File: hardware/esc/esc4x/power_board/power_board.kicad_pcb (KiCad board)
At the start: 4 copper layers, 44 x 46.5 mm, 107 parts, among them J1 Conn_01x06_MountingPin, J10 Conn_01x03_Pin, J2 Conn_01x01, J3 Conn_01x01, J4 Conn_01x03_Pin, J5 Conn_01x03_Pin, J6 Conn_01x03_Pin, Q1 BSC010N04LS6, Q10 BSC010N04LS6, Q11 BSC010N04LS6, Q12 BSC010N04LS6, Q13 BSC010N04LS6, Q14 BSC010N04LS6, Q15 BSC010N04LS6, Q16 BSC010N04LS6, Q17 BSC010N04LS6, Q18 BSC010N04LS6, Q19 BSC010N04LS6, Q2 BSC010N04LS6, Q20 BSC010N04LS6, Q21 BSC010N04LS6, Q22 BSC010N04LS6, Q23 BSC010N04LS6, Q24 BSC010N04LS6, Q3 BSC010N04LS6, Q4 BSC010N04LS6, Q5 BSC010N04LS6, Q6 BSC010N04LS6, Q7 BSC010N04LS6, Q8 BSC010N04LS6, Q9 BSC010N04LS6, U2 AP7381-50Y-13, U3 AP7381-33SA-7, U4 AP7381-50Y-13, U5 AP7381-50Y-13, U7 AP7381-33SA-7, U8 AP7381-50Y-13

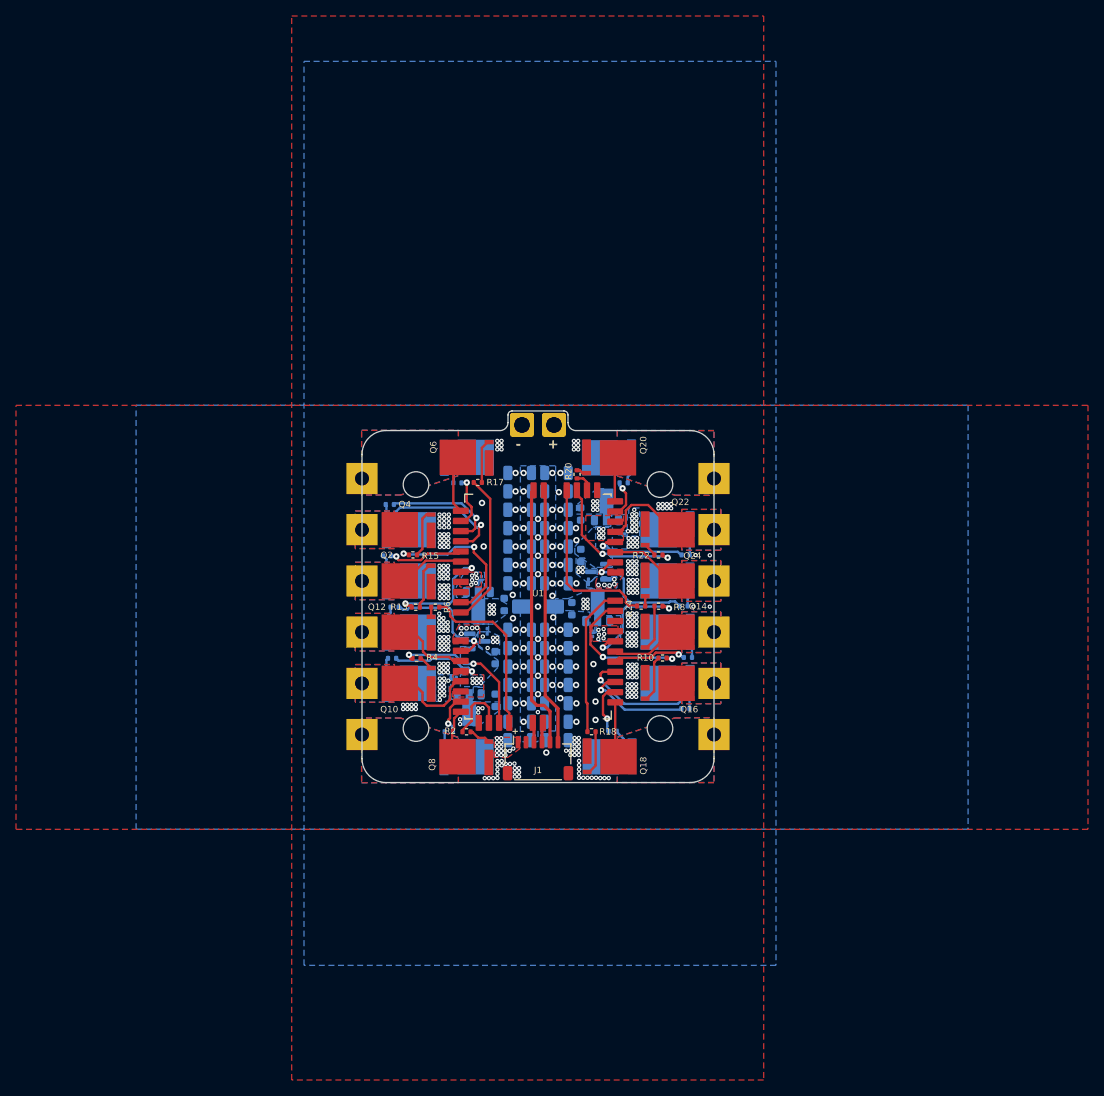
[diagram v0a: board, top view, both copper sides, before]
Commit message: Wider ESC battery holes
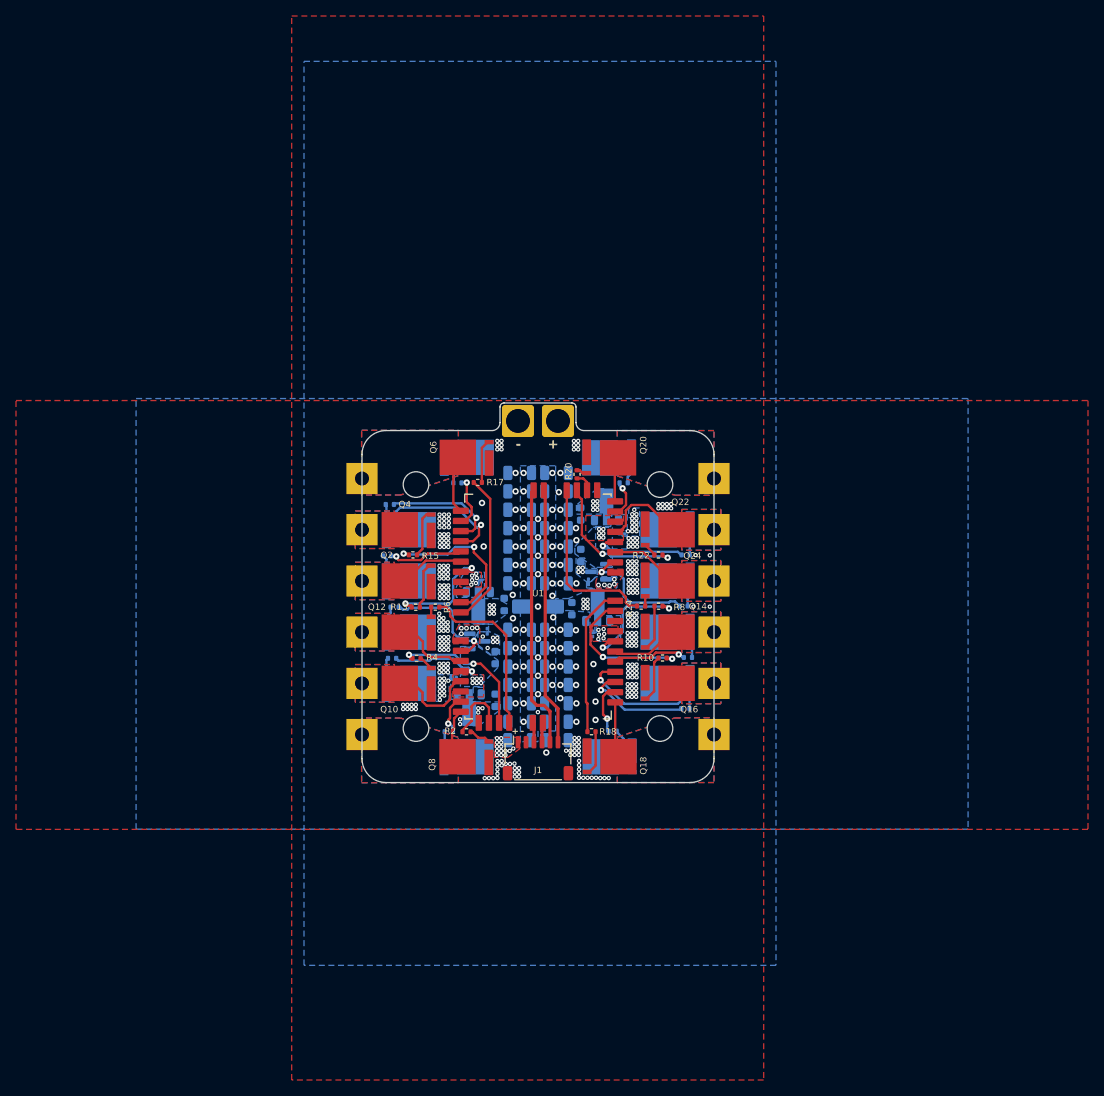
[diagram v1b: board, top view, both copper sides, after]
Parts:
- moved J2 0.71 mm to (152.5, 76.8)
- moved J3 0.71 mm to (147.5, 76.8)
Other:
- board size 44 x 46.5 mm -> 44 x 47.5 mm
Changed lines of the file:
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@@
 	(footprint "Custom:EscBatteryConnector"
 		(layer "F.Cu")
-		(at 152 77.3 90)
+		(at 152.5 76.8 90)
 		(descr "Soldered wire connection, for a single 1 mm² wire, basic insulation, conductor diameter 1.4mm, outer diameter 2.7mm, size source Multi-Contact FLEXI-E 1.0 (https://www.staubli.com/content/dam/ecs/catalogs-brochures/TM/CAB-Main-11014119-en.pdf#page=9), bend radius 3 times outer diameter, generated with kicad-footprint-generator")
 		(tags "connector wire 1sqmm")
@@
 		(sheetname "/")
 		(sheetfile "power_board.kicad_sch")
-		(units
-			(unit
-				(name "A")
-				(pins "1")
-			)
-		)
 		(attr exclude_from_bom)
 		(duplicate_pad_numbers_are_jumpers no)
@@
 		(pad "1" thru_hole roundrect
 			(at 0 0 90)
-			(size 3 3)
-			(drill 2)
+			(size 4 4)
+			(drill 3)
 			(layers "*.Cu" "*.Mask")
 			(remove_unused_layers no)
@@
 	(footprint "Custom:EscBatteryConnector"
 		(layer "F.Cu")
-		(at 148 77.3 90)
+		(at 147.5 76.8 90)
 		(descr "Soldered wire connection, for a single 1 mm² wire, basic insulation, conductor diameter 1.4mm, outer diameter 2.7mm, size source Multi-Contact FLEXI-E 1.0 (https://www.staubli.com/content/dam/ecs/catalogs-brochures/TM/CAB-Main-11014119-en.pdf#page=9), bend radius 3 times outer diameter, generated with kicad-footprint-generator")
 		(tags "connector wire 1sqmm")
@@
 		(sheetname "/")
 		(sheetfile "power_board.kicad_sch")
-		(units
-			(unit
-				(name "A")
-				(pins "1")
-			)
-		)
 		(attr exclude_from_bom)
 		(duplicate_pad_numbers_are_jumpers no)
@@
 		(pad "1" thru_hole roundrect
 			(at 0 0 90)
-			(size 3 3)
-			(drill 2)
+			(size 4 4)
+			(drill 3)
 			(layers "*.Cu" "*.Mask")
 			(remove_unused_layers no)
@@
 	(gr_line
 		(start 131 78)
-		(end 145.25 78)
+		(end 144.25 78)
 		(stroke
 			(width 0.05)
@@
 		(layer "Edge.Cuts")
 	)
-	(gr_line
-		(start 146 122)
-		(end 131 122)
+	(gr_arc
+		(start 145.25 75.05)
+		(mid 145.396447 74.696447)
+		(end 145.75 74.55)
 		(stroke
 			(width 0.05)
@@
 	)
 	(gr_arc
-		(start 146.25 76.05)
-		(mid 146.396447 75.696447)
-		(end 146.75 75.55)
+		(start 145.25 77)
+		(mid 144.957107 77.707107)
+		(end 144.25 78)
 		(stroke
 			(width 0.05)
@@
 		(layer "Edge.Cuts")
 	)
-	(gr_arc
-		(start 146.25 77)
-		(mid 145.957107 77.707107)
-		(end 145.25 78)
+	(gr_line
+		(start 145.25 77)
+		(end 145.25 75.05)
 		(stroke
 			(width 0.05)
@@
 	)
 	(gr_line
-		(start 146.25 77)
-		(end 146.25 76.05)
+		(start 145.75 74.55)
+		(end 154.25 74.55)
 		(stroke
 			(width 0.05)
@@
 	)
 	(gr_line
-		(start 146.75 75.55)
-		(end 153.25 75.55)
+		(start 146 122)
+		(end 131 122)
 		(stroke
 			(width 0.05)
@@
 	)
 	(gr_arc
-		(start 153.25 75.55)
-		(mid 153.603553 75.696447)
-		(end 153.75 76.05)
+		(start 154.25 74.55)
+		(mid 154.603553 74.696447)
+		(end 154.75 75.05)
 		(stroke
 			(width 0.05)
@@
 	)
 	(gr_line
-		(start 153.75 77)
-		(end 153.75 76.05)
+		(start 154.75 77)
+		(end 154.75 75.05)
 		(stroke
 			(width 0.05)
@@
 	)
 	(gr_arc
-		(start 154.75 78)
-		(mid 154.042893 77.707107)
-		(end 153.75 77)
+		(start 155.75 78)
+		(mid 155.042893 77.707107)
+		(end 154.75 77)
 		(stroke
 			(width 0.05)
@@
 	)
 	(gr_line
-		(start 154.75 78)
+		(start 155.75 78)
 		(end 169 78)
 		(stroke
@@
 		(polygon
 			(pts
-				(xy 84.75 74.85) (xy 218.75 74.85) (xy 218.75 127.85) (xy 84.75 127.85)
+				(xy 84.75 74.25) (xy 218.75 74.25) (xy 218.75 127.85) (xy 84.75 127.85)
 			)
 		)
@@
 		(polygon
 			(pts
-				(xy 99.76 74.83) (xy 203.76 74.83) (xy 203.76 127.83) (xy 99.76 127.83)
+				(xy 99.76 74) (xy 203.76 74) (xy 203.76 127.83) (xy 99.76 127.83)
 			)
 		)
